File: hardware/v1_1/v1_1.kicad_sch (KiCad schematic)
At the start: 81 parts, among them J1 AUDIO IN, J10 Additional Sensor, J11 MIDI out TRS, J12 MIDI in TRS, J13 MIDI thru TRS, J2 MIDI OUT, J3 MIDI IN, J4 MIDI THRU, J5 OUTPUT R, J6 OUTPUT L - MONO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

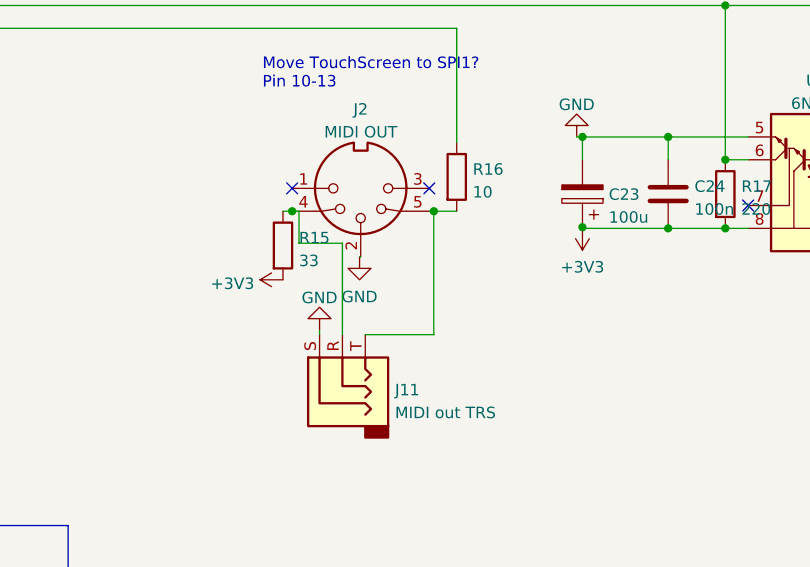
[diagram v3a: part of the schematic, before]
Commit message: Added test of several pot with lpf
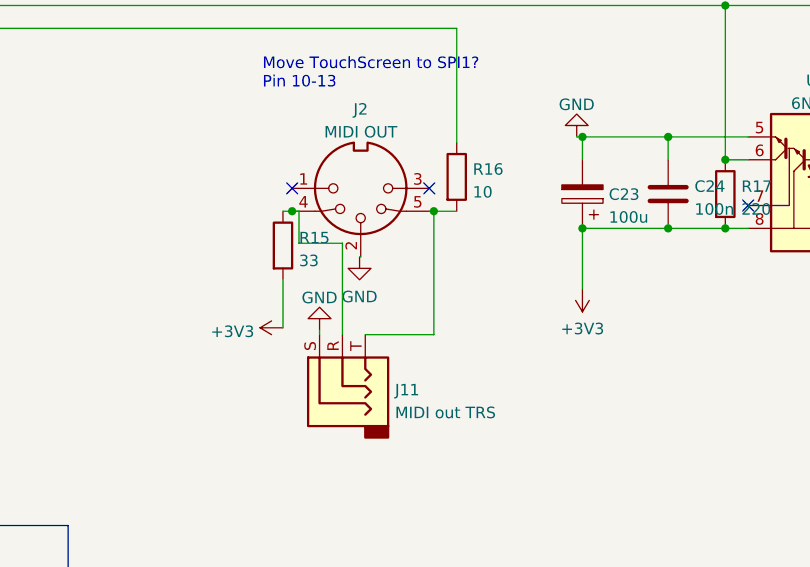
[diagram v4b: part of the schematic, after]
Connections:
- net +3V3: now also C23.1, C24.2, R17.2, U7.8 (VCC)
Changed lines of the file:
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@@
   (junction (at 444.5 60.325) (diameter 0) (color 0 0 0 0)
   )
-  (junction (at 191.77 137.668) (diameter 0) (color 0 0 0 0)
-  )
   (junction (at 457.835 59.69) (diameter 0) (color 0 0 0 0)
   )
@@
   )
   (junction (at 34.925 124.46) (diameter 0) (color 0 0 0 0)
+  )
+  (junction (at 191.77 137.795) (diameter 0) (color 0 0 0 0)
   )
   (junction (at 271.78 70.358) (diameter 0) (color 0 0 0 0)
@@
     (stroke (width 0) (type default) (color 0 0 0 0))
   )
+  (wire (pts (xy 191.77 137.795) (xy 191.77 137.668))
+    (stroke (width 0) (type default) (color 0 0 0 0))
+  )
   (polyline (pts (xy 59.69 123.825) (xy 81.915 123.825))
     (stroke (width 0) (type default) (color 0 0 0 0))
@@
     (stroke (width 0) (type default) (color 0 0 0 0))
   )
+  (wire (pts (xy 191.77 144.526) (xy 191.77 137.795))
+    (stroke (width 0) (type default) (color 0 0 0 0))
+  )
   (wire (pts (xy 51.435 143.51) (xy 31.115 143.51))
     (stroke (width 0) (type default) (color 0 0 0 0))
@@
   )
   (wire (pts (xy 163.195 26.67) (xy 163.195 30.48))
+    (stroke (width 0) (type default) (color 0 0 0 0))
+  )
+  (wire (pts (xy 158.496 148.844) (xy 158.496 143.51))
     (stroke (width 0) (type default) (color 0 0 0 0))
   )
@@
     (pin "2")
   )
-  (symbol (lib_id "power:+3V3") (at 191.77 137.668 180) (unit 1)
-    (in_bom yes) (on_board yes) (fields_autoplaced)
-    (property "Reference" "#PWR023" (id 0) (at 191.77 133.858 0)
-      (effects (font (size 1.27 1.27)) hide)
-    )
-    (property "Value" "+3V3" (id 1) (at 191.77 142.1114 0))
-    (property "Footprint" "" (id 2) (at 191.77 137.668 0)
-      (effects (font (size 1.27 1.27)) hide)
-    )
-    (property "Datasheet" "" (id 3) (at 191.77 137.668 0)
+  (symbol (lib_id "power:+3V3") (at 191.77 144.526 180) (unit 1)
+    (in_bom yes) (on_board yes) (fields_autoplaced)
+    (property "Reference" "#PWR023" (id 0) (at 191.77 140.716 0)
+      (effects (font (size 1.27 1.27)) hide)
+    )
+    (property "Value" "+3V3" (id 1) (at 191.77 148.9694 0))
+    (property "Footprint" "" (id 2) (at 191.77 144.526 0)
+      (effects (font (size 1.27 1.27)) hide)
+    )
+    (property "Datasheet" "" (id 3) (at 191.77 144.526 0)
       (effects (font (size 1.27 1.27)) hide)
     )
@@
     (pin "1")
   )
-  (symbol (lib_id "power:+3V3") (at 158.496 143.51 90) (unit 1)
-    (in_bom yes) (on_board yes) (fields_autoplaced)
-    (property "Reference" "#PWR022" (id 0) (at 162.306 143.51 0)
-      (effects (font (size 1.27 1.27)) hide)
-    )
-    (property "Value" "+3V3" (id 1) (at 155.321 143.9438 90)
+  (symbol (lib_id "power:+3V3") (at 158.496 148.844 90) (unit 1)
+    (in_bom yes) (on_board yes) (fields_autoplaced)
+    (property "Reference" "#PWR022" (id 0) (at 162.306 148.844 0)
+      (effects (font (size 1.27 1.27)) hide)
+    )
+    (property "Value" "+3V3" (id 1) (at 155.321 149.2778 90)
       (effects (font (size 1.27 1.27)) (justify left))
     )
-    (property "Footprint" "" (id 2) (at 158.496 143.51 0)
-      (effects (font (size 1.27 1.27)) hide)
-    )
-    (property "Datasheet" "" (id 3) (at 158.496 143.51 0)
-      (effects (font (size 1.27 1.27)) hide)
-    )
+    (property "Footprint" "" (id 2) (at 158.496 148.844 0)
+      (effects (font (size 1.27 1.27)) hide)
+    )
+    (property "Datasheet" "" (id 3) (at 158.496 148.844 0)
+      (effects (font (size 1.27 1.27)) hide)
+    )
